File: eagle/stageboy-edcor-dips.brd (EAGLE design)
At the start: 120 x 75 mm, 39 parts, among them IC1 MEGA8-P, IC2 7805TV, J1 PWR, Q1 16MHz, X1 MIDI IN, X2 MIDI OUT, X4 22-23-2021, X6 GBIO

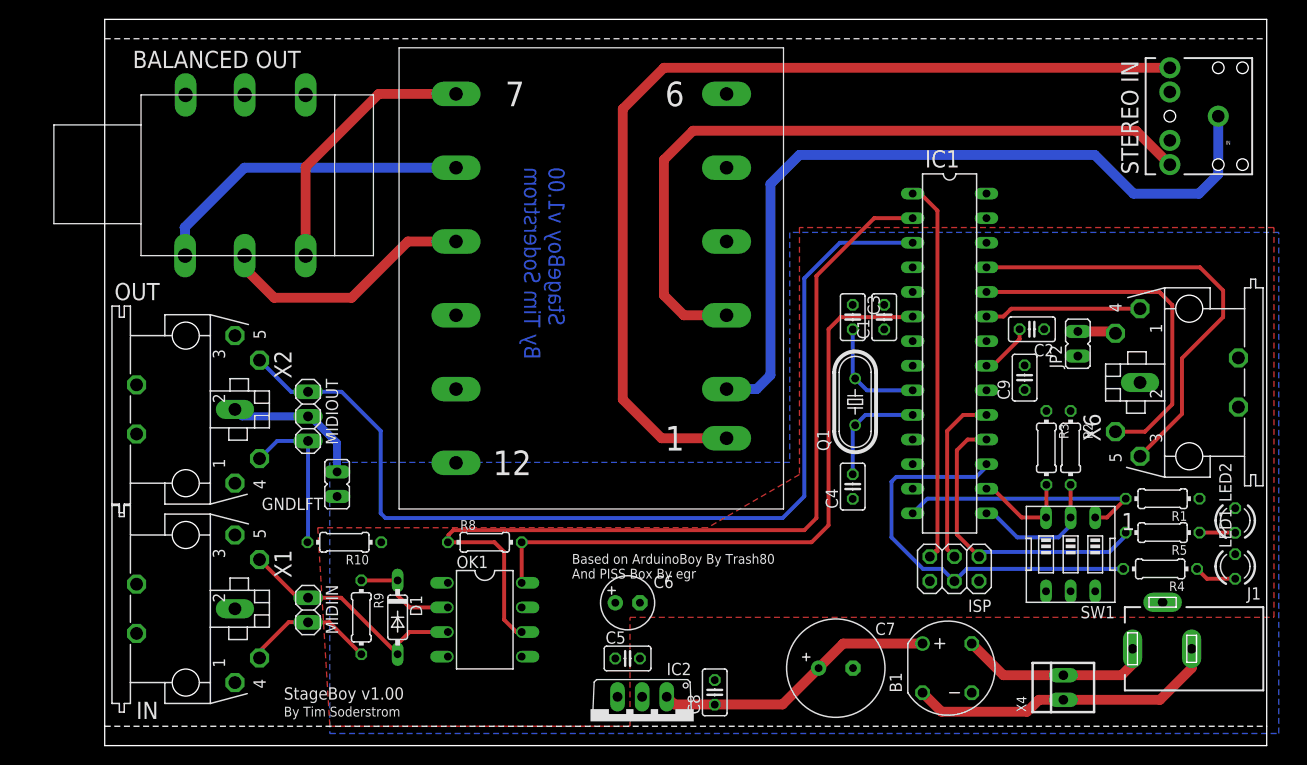
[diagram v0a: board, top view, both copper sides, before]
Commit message: Layout Optimizations
Moved the TRS jack towards the edge more.
Adjusted positions on audio-in, GB in, and LEDs.
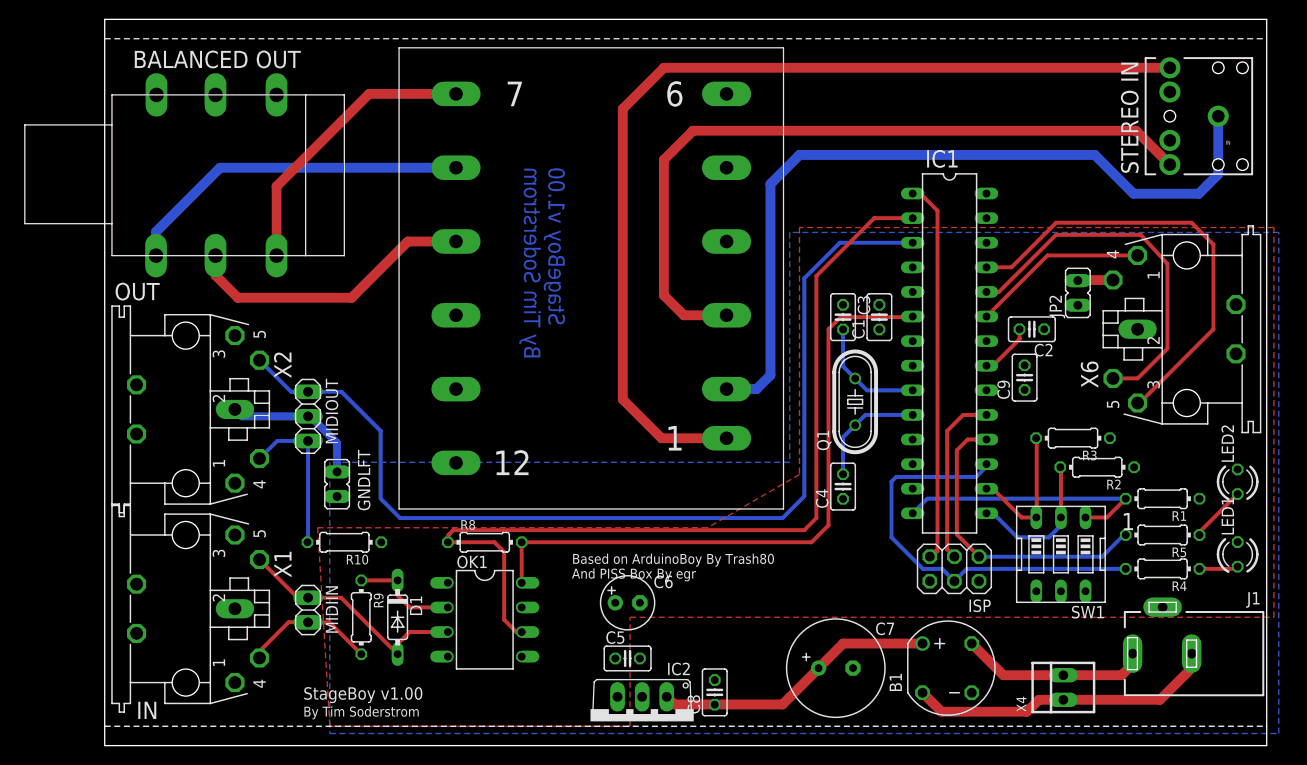
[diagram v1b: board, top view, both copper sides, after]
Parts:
- moved X6 5.51 mm to (111.8, 43.0)
- moved JP2 5.25 mm to (100.5, 46.8)
- moved LED2 4.01 mm to (117.0, 27.2)
- moved R2 3.40 mm to (102.5, 28.8), turned to 180 degrees
- moved OUT 3.00 mm to (24.8, 59.0)
- moved R3 2.93 mm to (100.0, 31.8), turned to 180 degrees
- moved LED1 1.27 mm to (117.0, 19.8)
- moved C3 1.00 mm to (76.2, 44.2)
- moved C4 1.00 mm to (76.2, 26.8)
- moved SW1 1.00 mm to (98.8, 19.8)
- moved C1 0.50 mm to (80.0, 44.2)
- moved J1 0.50 mm to (109.2, 9.50)
- moved R4 0.25 mm to (109.2, 18.2)
- moved R5 0.25 mm to (109.2, 21.8)
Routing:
- net N$15: track 10.8 -> 14.6 mm
- net N$33: track 26.8 -> 30.2 mm
- net N$30: track 33.5 -> 36.2 mm
- net N$3: track 3.70 -> 5.86 mm
- net N$26: track 16.2 -> 18.2 mm
- net N$32: track 27.8 -> 29.6 mm
- net N$25: track 37.0 -> 38.1 mm
- net N$4: track 26.6 -> 27.6 mm
- net N$21: track 104.1 -> 103.3 mm
- net N$14: track 14.4 -> 15.3 mm
- net N$24: track 11.6 -> 12.4 mm
- net N$22: track 11.6 -> 12.3 mm
- net N$38: track 32.5 -> 32.0 mm

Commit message: Added 5VDC Header
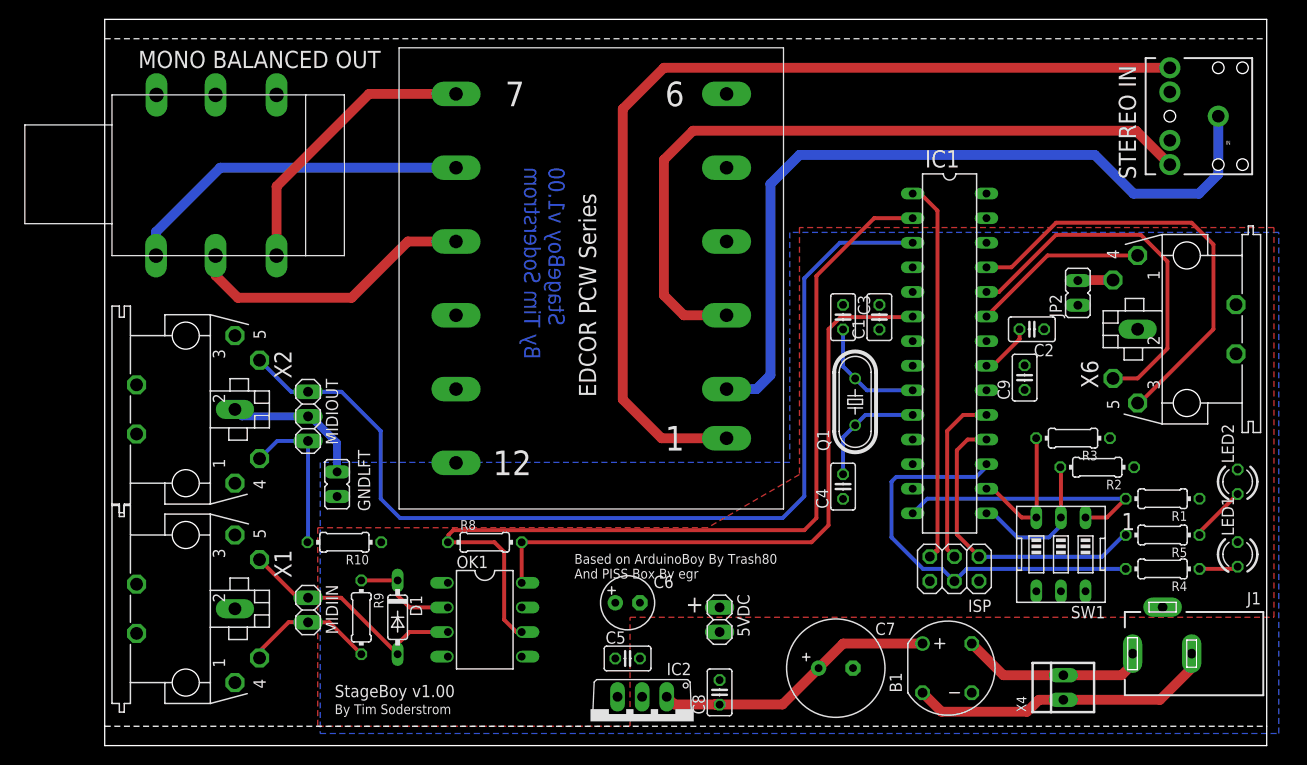
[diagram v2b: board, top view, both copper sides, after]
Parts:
- added 5VDC: DCPWR, pinhead:1X02
- moved C8 0.50 mm to (63.5, 5.50)
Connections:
- net +5V: now also 5VDC.1
- net GND: now also 5VDC.2
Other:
- board text added: "+"
- board text added: "EDCOR PCW Series"
- board text added: "MONO BALANCED OUT"
- board text removed: "BALANCED OUT"
- board text removed: "IN"
- board text removed: "OUT"
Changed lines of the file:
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@@
 <text x="47.5" y="59.75" size="1.6764" layer="16" font="vector" ratio="15" rot="MR270">StageBoy v1.00
 By Tim Soderstrom</text>
-<text x="20.5" y="4.75" size="1.27" layer="25" font="vector">StageBoy v1.00</text>
-<text x="20.5" y="3" size="1.016" layer="25" font="vector">By Tim Soderstrom</text>
-<text x="48.25" y="17.25" size="1.016" layer="25" font="vector">Based on ArduinoBoy By Trash80
+<text x="23.75" y="5" size="1.27" layer="25" font="vector">StageBoy v1.00</text>
+<text x="23.75" y="3.25" size="1.016" layer="25" font="vector">By Tim Soderstrom</text>
+<text x="48.5" y="17.25" size="1.016" layer="25" font="vector">Based on ArduinoBoy By Trash80
 And PISS Box By egr
 </text>
-<text x="3.25" y="2.75" size="1.778" layer="25">IN</text>
-<text x="1" y="46" size="1.778" layer="25">OUT</text>
-<text x="106.75" y="59" size="1.778" layer="25" rot="R90">STEREO IN</text>
-<text x="20.25" y="71.75" size="1.778" layer="25" rot="R180">BALANCED OUT</text>
+<text x="106.5" y="58.5" size="1.778" layer="25" rot="R90">STEREO IN</text>
+<text x="28.5" y="71.75" size="1.778" layer="25" rot="R180">MONO BALANCED OUT</text>
 <text x="105" y="22.25" size="1.778" layer="25">1</text>
+<text x="50.75" y="36" size="1.778" layer="25" rot="R90">EDCOR PCW Series</text>
+<text x="60" y="13.75" size="1.778" layer="25">+</text>
 </plain>
 <attributes>
@@
 <element name="B1" library="rectifier" package="RB1A" value="B1" x="87" y="8"/>
 <element name="C7" library="resistor" package="E3,5-10" value="2200uF" x="75.5" y="8"/>
-<element name="C8" library="rcl" package="C025-025X050" value="330nF" x="63" y="5.5" rot="R90"/>
+<element name="C8" library="rcl" package="C025-025X050" value="330nF" x="63.5" y="5.5" rot="R90"/>
 <element name="OUT" library="Neutrik" package="NMJ6HFD2" value="NMJ6HFD2" x="24.75" y="59" rot="R90"/>
 <element name="GNDLFT" library="jumper" package="JP1" value="GNDLIFT" x="24" y="27" smashed="yes" rot="R180">
@@
 <element name="R4" library="resistor" package="0204/7" value="220" x="109.25" y="18.25" rot="R180"/>
 <element name="R5" library="resistor" package="0204/7" value="220" x="109.25" y="21.75" rot="R180"/>
+<element name="5VDC" library="pinhead" package="1X02" value="DCPWR" x="63.5" y="13" rot="R270"/>
 </elements>
 <signals>
@@
 <vertex x="70.75" y="53"/>
 <vertex x="70.75" y="29.25"/>
-<vertex x="23.25" y="29.25"/>
-<vertex x="23.25" y="1.25"/>
+<vertex x="22.25" y="29.25"/>
+<vertex x="22.25" y="1.25"/>
 <vertex x="121.25" y="1.25"/>
 </polygon>
@@
 <contactref element="LED1" pad="K"/>
 <contactref element="LED2" pad="K"/>
+<contactref element="5VDC" pad="2"/>
 </signal>
 <signal name="+5V">
@@
 <vertex x="62.25" y="22.5"/>
 <vertex x="22" y="22.5"/>
-<vertex x="23.25" y="2"/>
+<vertex x="22" y="2"/>
 <vertex x="54.25" y="2"/>
 <vertex x="54.25" y="13.25"/>
@@
 <contactref element="SW1" pad="4"/>
 <contactref element="SW1" pad="5"/>
+<contactref element="5VDC" pad="1"/>
 </signal>
 <signal name="N$2">
@@
 <wire x1="106.67" y1="35.38" x2="106.88" y2="35.38" width="0.4064" layer="1"/>
 <wire x1="106.88" y1="35.38" x2="114.5" y2="43" width="0.4064" layer="1"/>
-<wire x1="112.25" y1="54" x2="114.5" y2="51.75" width="0.4064" layer="1"/>
+<wire x1="114.5" y1="51.75" x2="112.25" y2="54" width="0.4064" layer="1"/>
 </signal>
 <signal name="N$25">
@@
 <wire x1="98.25" y1="52.75" x2="92.35" y2="46.85" width="0.4064" layer="1"/>
 <wire x1="91.06" y1="46.85" x2="92.35" y2="46.85" width="0.4064" layer="1"/>
-<wire x1="109.75" y1="41" x2="109.75" y2="49.75" width="0.4064" layer="1"/>
-<wire x1="109.75" y1="49.75" x2="107" y2="52.75" width="0.4064" layer="1"/>
+<wire x1="109.75" y1="41" x2="109.75" y2="50" width="0.4064" layer="1"/>
+<wire x1="109.75" y1="50" x2="107" y2="52.75" width="0.4064" layer="1"/>
 </signal>
 <signal name="N$26">
@@
 <wire x1="73.722" y1="7.972" x2="70" y2="4.25" width="1.016" layer="1"/>
 <wire x1="70" y1="4.25" x2="63.02" y2="4.25" width="1.016" layer="1"/>
-<wire x1="63.02" y1="4.25" x2="63" y2="4.23" width="1.016" layer="1"/>
+<wire x1="63.02" y1="4.25" x2="63.5" y2="4.23" width="1.016" layer="1"/>
 <wire x1="63.02" y1="4.25" x2="58.83" y2="4.25" width="1.016" layer="1"/>
 <wire x1="58.83" y1="4.25" x2="58.04" y2="5.04" width="1.016" layer="1"/>

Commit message: Added 5VDC Header
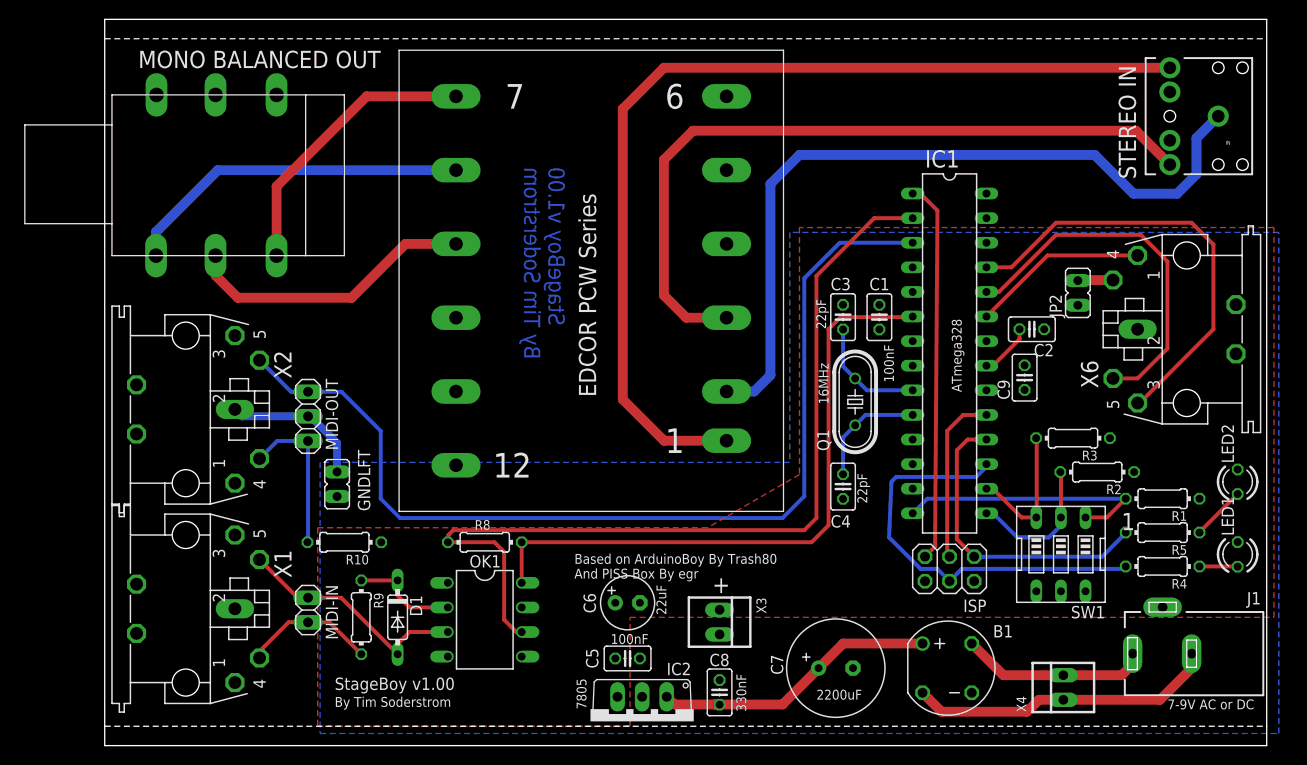
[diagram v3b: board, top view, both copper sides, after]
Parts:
- removed 5VDC: DCPWR, pinhead:1X02
- added X3: DCPWR, con-molex:22-23-2021
- moved ISP 0.50 mm to (87.2, 18.2)
- moved R2 0.50 mm to (102.5, 28.2)
- moved R4 0.25 mm to (109.2, 18.5)
- moved R5 0.25 mm to (109.2, 22.0)
- moved U$1 0.25 mm to (50.2, 48.0)
- renumbered MIDIIN to MIDI-IN, MIDIOUT to MIDI-OUT
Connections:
- net +5V: now also X3.1; no longer 5VDC.1
- net GND: now also X3.2; no longer 5VDC.2
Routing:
- net N$35: track 80.9 -> 79.6 mm
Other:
- board text added: "100nF"
- board text added: "16MHz"
- board text added: "2200uF"
- board text added: "22pF"
- board text added: "22uF"
- board text added: "330nF"
- board text added: "7-9V AC or DC"
- board text added: "7805"
- board text added: "ATmega328"

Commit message: Added side panels, minor layout changes to board
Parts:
- removed J1: PWR, con-jack:DCJ0303
- removed LED1: (no value), led:LED3MM
- removed R4: 220, resistor:0204/7
- added J2: DCJ0202, con-jack:DCJ0202
- moved LED2 4.25 mm to (115.0, 23.5)
- moved R1 4.12 mm to (105.2, 26.5)
- moved R5 2.61 mm to (108.5, 19.5)
- moved R2 1.75 mm to (102.5, 30.0)
- moved R3 1.75 mm to (100.0, 33.5)
- moved GNDLFT 0.50 mm to (24.0, 26.5)
- moved X1 0.17 mm to (8.25, 14.2)
- moved X2 0.12 mm to (8.25, 34.8)
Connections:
- removed net N$5: LED1.A, R4.1
- net GND: no longer LED1.K
- net N$17: no longer R4.2
- net N$38: now also J2.3; no longer J1.3
- net N$39: now also J2.1; no longer J1.1
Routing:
- net N$17: track 43.4 -> 24.6 mm
- net N$4: track 27.6 -> 22.0 mm
- net N$21: track 103.3 -> 98.6 mm
- net N$5: track 3.95 -> 0.00 mm
- net N$27: track 16.2 -> 13.7 mm
- net N$18: track 31.9 -> 30.1 mm
- net N$3: track 5.61 -> 3.84 mm
- net N$15: track 14.6 -> 16.3 mm
- net N$13: track 11.0 -> 10.1 mm
- net N$38: track 32.0 -> 32.8 mm
- net N$14: track 15.6 -> 16.5 mm
- net N$43: track 15.0 -> 14.4 mm

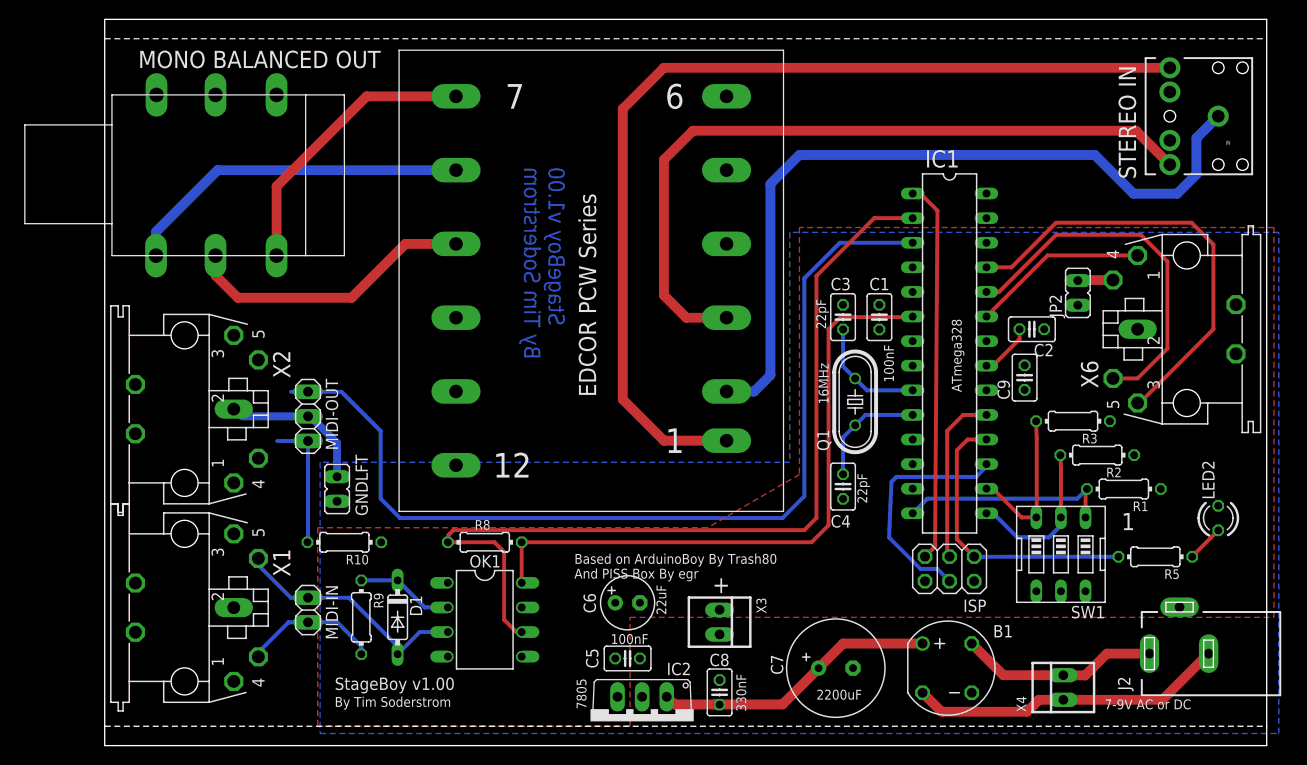
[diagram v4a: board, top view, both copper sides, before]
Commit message: Added silkscreen and made minor formatting changes
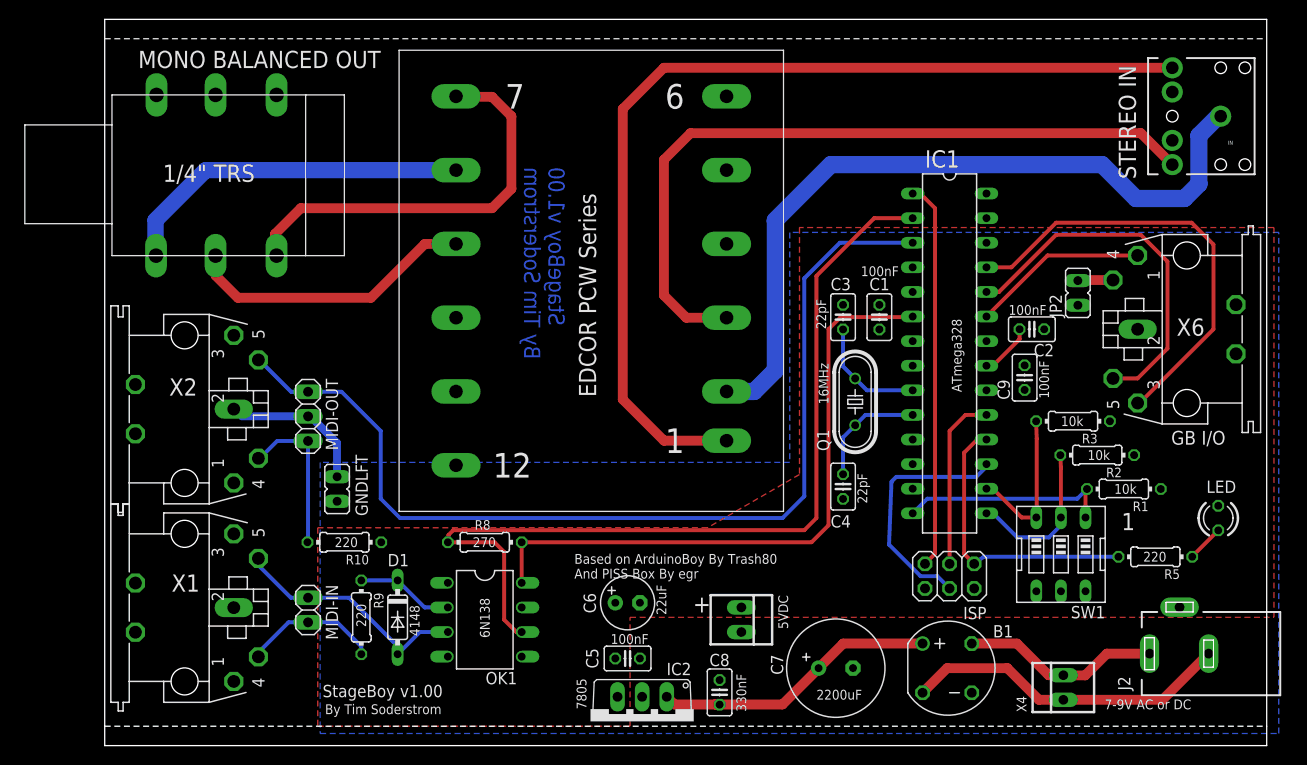
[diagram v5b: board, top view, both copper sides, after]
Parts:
- removed X3: DCPWR, con-molex:22-23-2021
- added 5VDC: DCPWR, con-molex:22-23-2021
- R10: value R10 -> 220
- R8: value R8 -> 270
- R9: value R9 -> 220
- moved ISP 0.75 mm to (87.2, 17.5)
- moved IN 0.25 mm to (115.2, 65.0)
- renumbered LED2 to LED
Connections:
- net +5V: now also 5VDC.1; no longer X3.1
- net GND: now also 5VDC.2; no longer X3.2
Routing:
- net N$32: track 29.5 -> 42.6 mm
- net N$21: track 98.6 -> 103.4 mm
- net N$27: track 13.7 -> 16.4 mm
- net N$35: track 79.6 -> 77.7 mm
- net N$38: track 32.8 -> 33.9 mm
- net N$30: track 36.1 -> 36.8 mm
- net N$17: track 24.6 -> 25.3 mm
- net N$12: track 24.8 -> 25.5 mm
- net N$1: track 39.5 -> 40.1 mm
- net N$16: track 13.8 -> 14.4 mm
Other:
- board text added: "1/4" TRS"
- board text added: "10k"
- board text added: "220"
- board text added: "270"
- board text added: "4148"
- board text added: "6N138"
- board text added: "GB I/O"
